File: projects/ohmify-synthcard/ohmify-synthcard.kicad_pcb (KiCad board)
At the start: 2 copper layers, 68.6 x 45.7 mm, 10 parts, among them U1 NE555P, U2 NE555P

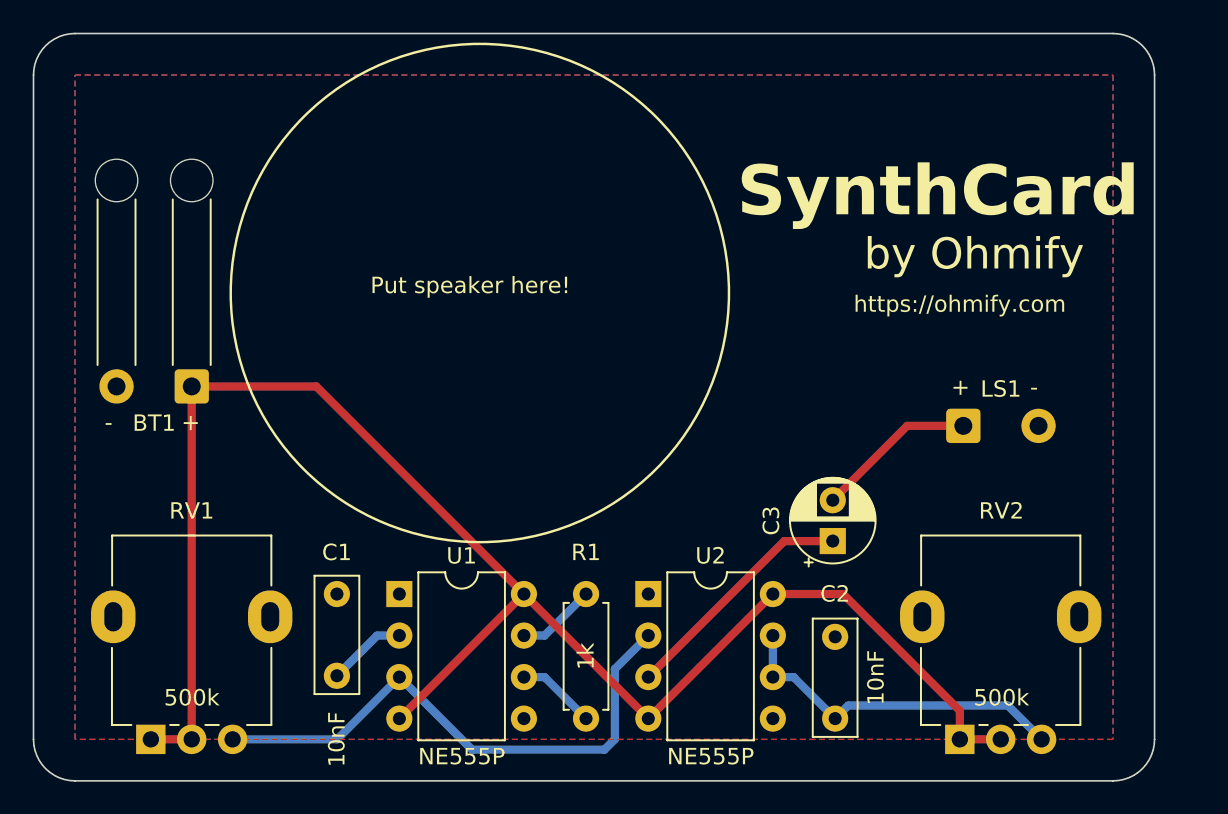
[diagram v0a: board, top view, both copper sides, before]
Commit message: Fixed synthcard, added new gerber files
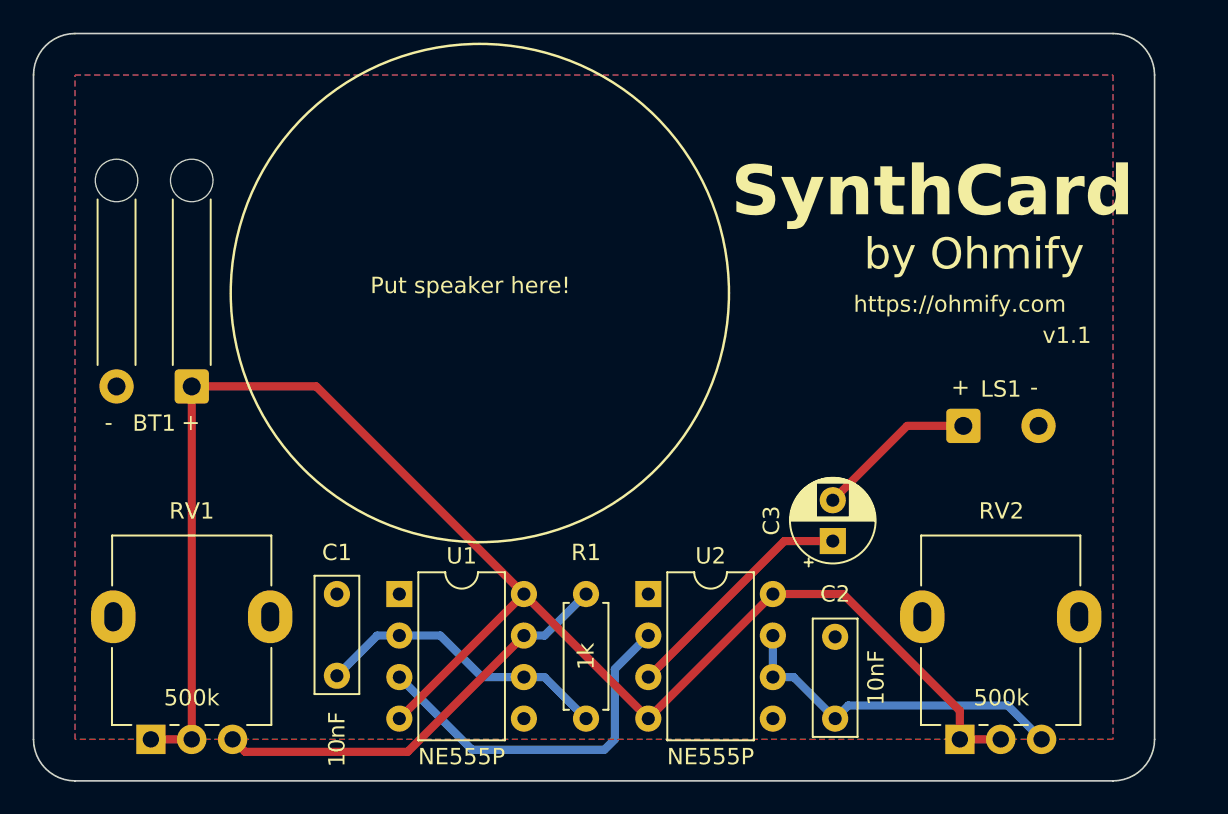
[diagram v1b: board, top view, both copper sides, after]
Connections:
- C1 pad 1: Net-(U1-TR) -> Net-(U1-THR)
- RV1 pad 3: Net-(U1-Q) -> Net-(U1-DIS)
- U1 pad 2: Net-(U1-TR) -> Net-(U1-THR)
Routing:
- net Net-(U1-DIS): track 4.85 -> 25.9 mm
- net Net-(U1-THR): track 4.85 -> 18.4 mm
- net Net-(U1-Q): track 34.3 -> 22.5 mm
- net Net-(U1-TR): track 4.84 -> 0.00 mm
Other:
- board text added: "v1.1"
